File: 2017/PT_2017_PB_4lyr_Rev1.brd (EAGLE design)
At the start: 162.5 x 209.5 mm, 162 parts, among them J1 APP_2POS_CONFIG12V_VERT, J2 APP_2POS_CONFIG12V_VERT, J3 APP_2POS_CONFIG12V_VERT, J4 APP_2POS_CONFIG12V_VERT, Q1 Q_IRFS7437PbF, Q10 MOSFET-NCHANNELFDD8780, Q11 MOSFET-NCHANNELFDD8780, Q12 2N7002, Q13 2N7002PW, Q2 Q_IRFS7437PbF, Q3 Q_IRFS7437PbF, Q4 Q_IRFS7437PbF, Q5 Q_IRFS7437PbF, Q6 Q_IRFS7437PbF, Q7 Q_IRFS7437PbF, Q8 MOSFET-NCHANNELFDD8780, Q9 MOSFET-NCHANNELFDD8780, U1 LT1910, U10 ACS722LLCTR-40AU-T, U11 ACS722LLCTR-40AU-T, U12 ACS722LLCTR-40AU-T, U13 ACS722LLCTR-40AU-T, U14 ACS722LLCTR-40AU-T, U15 LM5050, U16 LM5050, U17 LM5050, U18 LM5050, U19 ACS722LLCTR-40AU-T, U2 LT1910, U20 ACS722LLCTR-40AU-T, U21 ACS722LLCTR-40AU-T, U22 ACS722LLCTR-40AU-T, U24 MAX3077, U3 LT1910, U4 LT1910, U5 LT1910, U6 LT1910, U7 LT1910, U8 ACS722LLCTR-40AU-T, U9 ACS722LLCTR-40AU-T, X1 22-23-2021

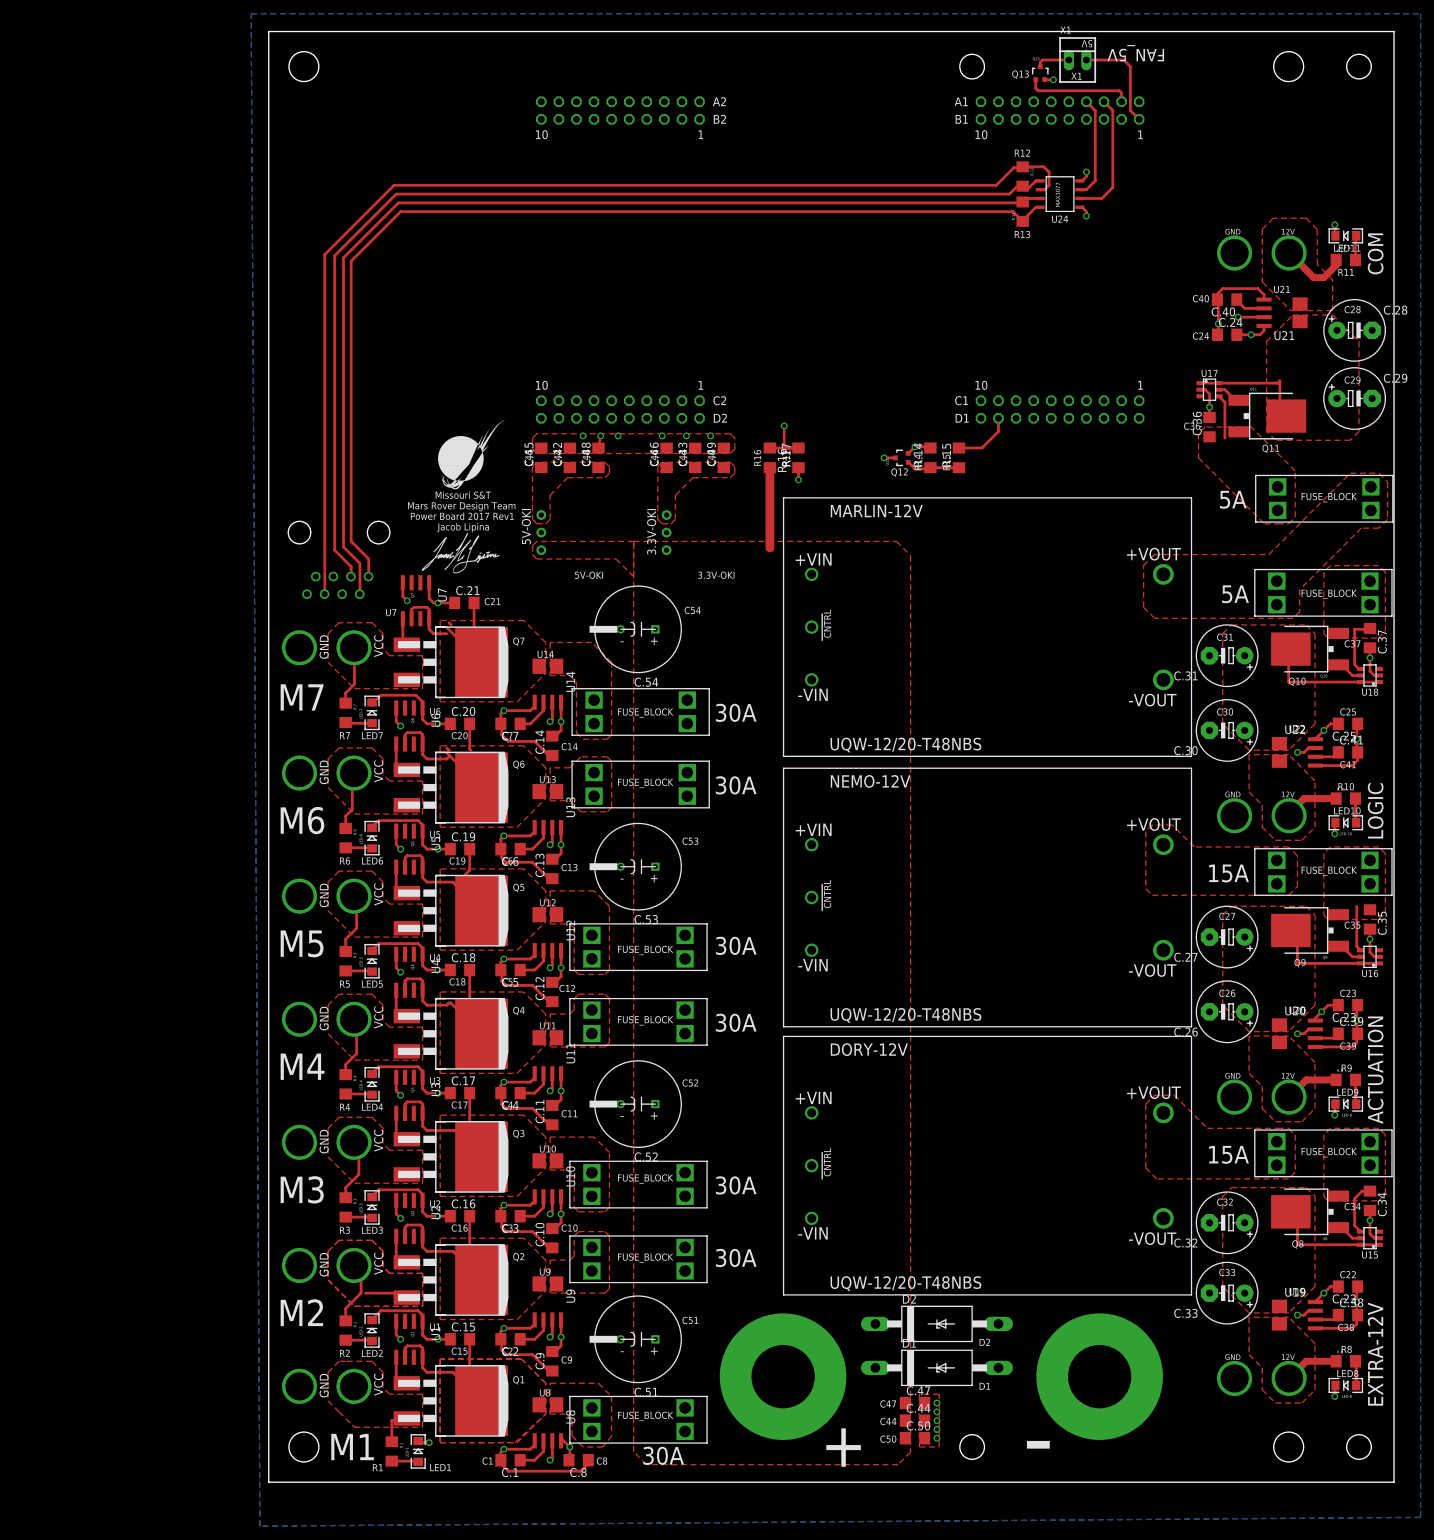
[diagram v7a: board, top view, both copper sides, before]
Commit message: Completed All Changes Adressed in Board Review
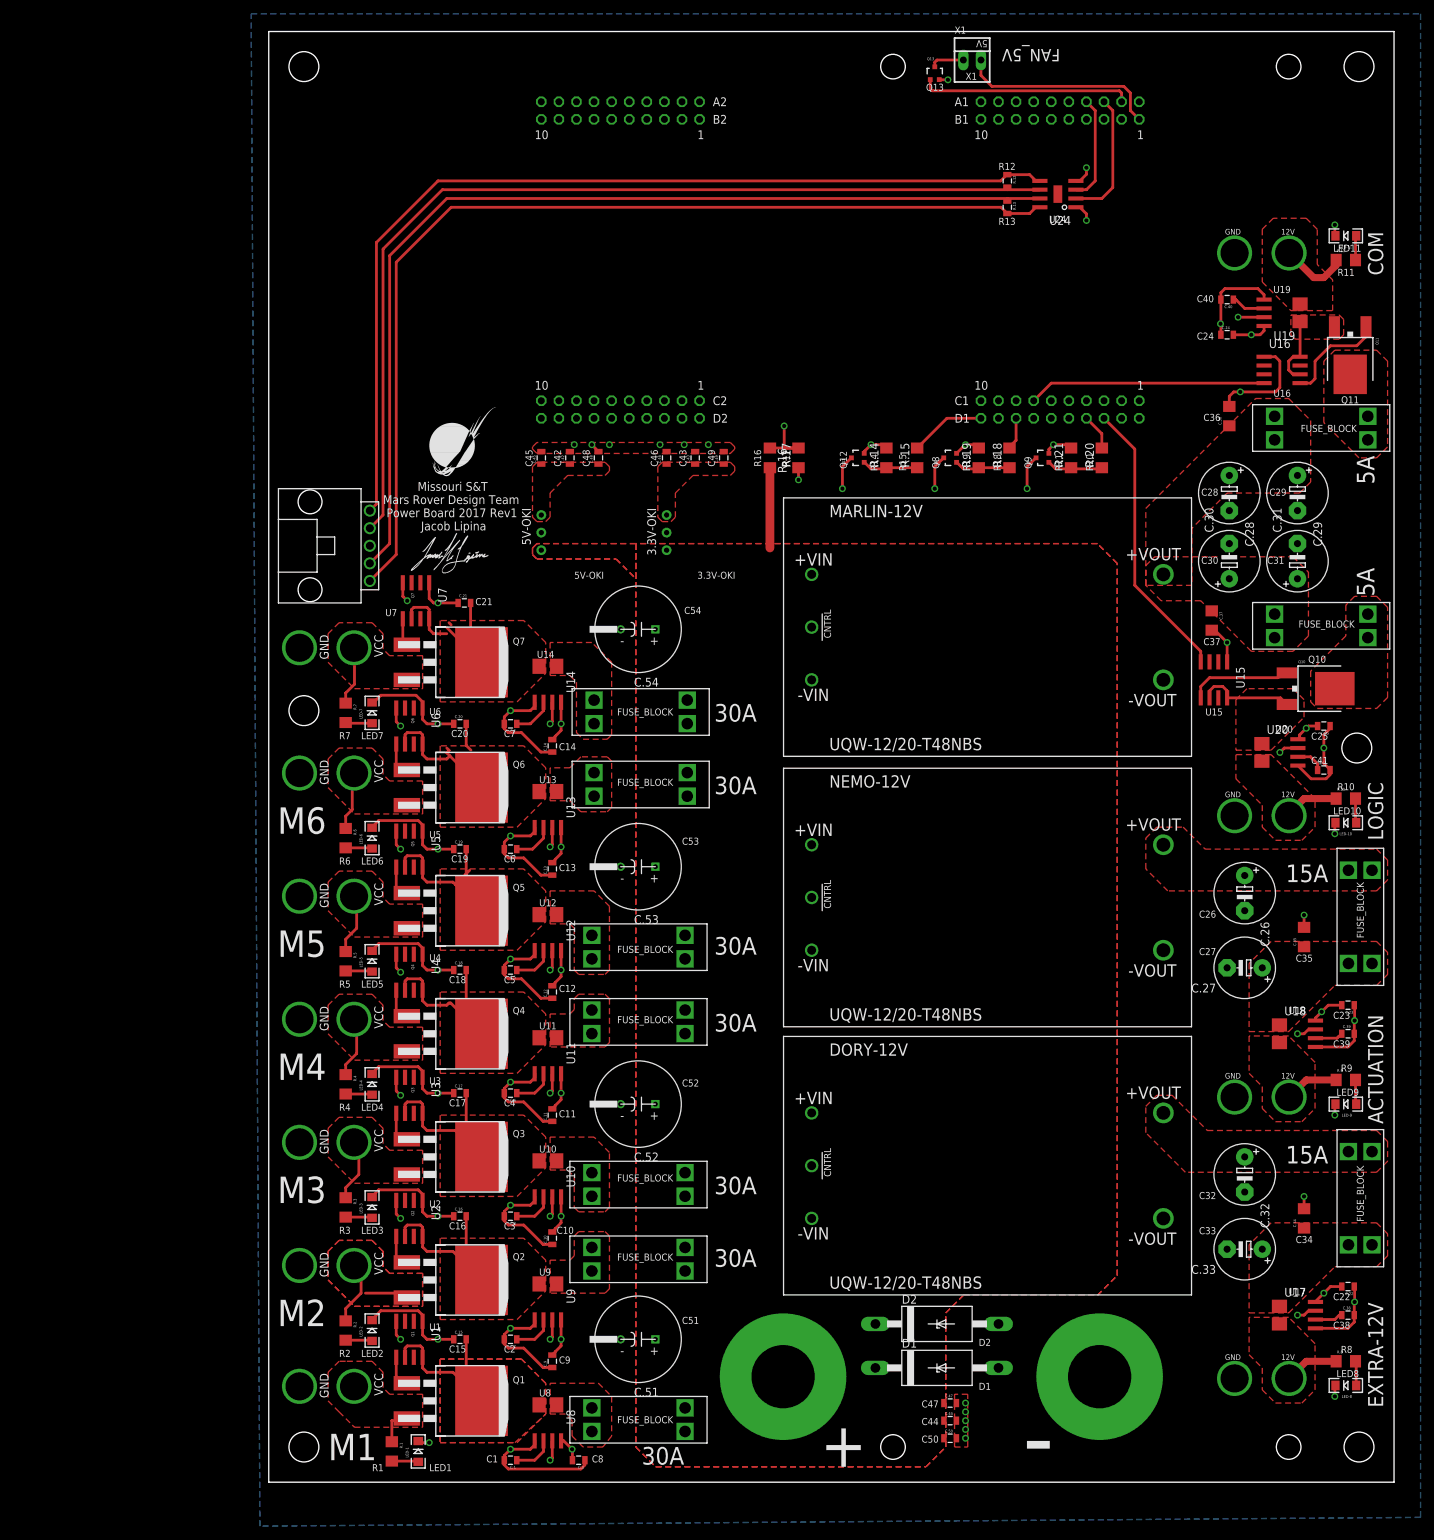
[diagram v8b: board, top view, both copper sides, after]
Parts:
- removed RJ45: RJ45KEYSTONE-949, MRDT-2015-General:KEYSTONE-949
- removed U21, U22: ACS722LLCTR-40AU-T, MRDT-2015-PowerBoard:SOIC8_ACS711
- added R.18, R.20: 1k, resistor:R1206
- added R.19, R.21: 100k, resistor:R1206
- added U$4, U$9: MOUNTING_HOLE#8, MRDT-Hardware:#8_SCREW
- added U$6: 5PIN, Molex-SL:5PIN
- C.1, C.10, C.11, C.12, C.13, C.14, C.15, C.16, C.17, C.18, C.19, C.2, C.20, C.21, C.22, C.23, C.24, C.25, C.3, C.38, C.39, C.4, C.40, C.41, C.42, C.43, C.44, C.45, C.46, C.47, C.48, C.49, C.5, C.50, C.6, C.7, C.8, C.9: device resistor:C1206 -> SparkFun-Capacitors:0805
- C.34, C.35, C.36, C.37: value 47uF -> 2.2uF; device resistor:C1206 -> SparkFun-Capacitors:1206
- Q8, Q9: value MOSFET-NCHANNELFDD8780 -> 2N7002; device SparkFun-DiscreteSemi:DPAK -> SparkFun-DiscreteSemi:SOT323
- R.12, R.13: value 120 Ohm -> 120; device SparkFun-Passives:1206 -> SparkFun-Passives:0805
- U15, U16: value LM5050 -> LT1910; device LM5050:LM5050 -> Jake:SO8
- U17, U18: value LM5050 -> ACS722LLCTR-40AU-T; device LM5050:LM5050 -> MRDT-2015-PowerBoard:SOIC8_ACS711
- U24: device MAX3077:MAX3070E -> MRDT-2015-General:SO8
- moved U19 144.8 mm to (146.4, 168.9), turned to 90 degrees
- moved U17 134.3 mm to (148.6, 24.1)
- moved Q8 120.2 mm to (98.4, 148.0)
- moved U16 85.7 mm to (146.4, 160.7), turned to 270 degrees
- moved U15 83.7 mm to (136.5, 115.9), turned to 180 degrees
- moved Q9 77.9 mm to (111.8, 148.0)
- moved U18 52.8 mm to (148.6, 64.8), turned to 270 degrees
- moved U20 40.7 mm to (146.1, 105.4)
- moved C.28 29.7 mm to (138.7, 142.9), turned to 270 degrees
- moved C.30 24.4 mm to (138.7, 133.0), turned to 90 degrees
- moved C.37 23.0 mm to (136.2, 124.5)
- moved U$31 19.7 mm to (161.9, 148.9), turned to 180 degrees
- moved C.26 17.3 mm to (141.0, 85.1), turned to 270 degrees
- moved C.31 17.0 mm to (148.6, 133.0), turned to 90 degrees
- moved C.29 16.0 mm to (148.6, 142.9), turned to 270 degrees
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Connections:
- removed net ACT-12V-SIG: U$1.PE2, U20.7
- removed net COM-12V-SIG: U$1.PE1, U22.7
- removed net EXTRA-12V-SIG: U$1.PE3, U19.7
- removed net LOGIC-12V-SIG: U$1.PE0, U21.7
- removed net N$11: C.32.+, C.33.+, Q8.4, U15.P$4, U15.P$5, U19.1
- removed net N$13: C.36.1, Q11.3, U$31.OUT_1, U$31.OUT_2, U17.P$6
- removed net N$14: C.26.+, C.27.+, Q9.4, U16.P$4, U16.P$5, U20.1
- removed net N$24: MARLIN-12V.8, U$31.IN_1, U$31.IN_2, U$32.IN_1, U$32.IN_2
- removed net REC+1: R.13.1, RJ45.P$1, U24.A
- removed net REC-1: R.13.2, RJ45.P$2, U24.B
- removed net SIG-12V: R.15.2, U$1.PN3
- removed net TRANS+1: R.12.2, RJ45.P$3, U24.Y
- removed net TRANS-1: R.12.1, RJ45.P$6, U24.Z
- new net ACT-CTL: R.18.2, U$1.PN2
- new net COM-SIG: U$1.PL0, U16.4
- new net COM/LOGIC-CTL: R.15.2, U$1.PP2
- new net EXTRA-CTL: R.20.2, U$1.PH3
- new net IMEAS-ACT: U$1.PE2, U18.7
- new net IMEAS-COM: U$1.PE0, U19.7
- new net IMEAS-EXTRA: U$1.PE3, U17.7
- new net IMEAS-LOGIC: U$1.PE1, U20.7
- new net LOGIC-SIG: U$1.PH2, U15.4
- new net N$18: C.27.+, C.35.1, U$30.OUT_1, U$30.OUT_2, U18.1
- new net N$25: Q8.1, R.18.1, R.19.1
- new net N$26: R.13.2, U$6.5, U24.8
- new net N$27: Q9.1, R.20.1, R.21.1
- new net N$28: Q10.1, U15.5
- new net N$29: R.13.1, U$6.4, U24.7
- new net N$30: R.12.2, U$6.2, U24.6
- new net N$31: R.12.1, U$6.1, U24.5
- net 12V-AUX-ACT: now also U18.4; no longer U20.4
- net 12V-AUX-COM: now also U20.4; no longer U22.4
- net 12V-AUX-EXTRA: now also U17.4; no longer U19.4
- net 12V-AUX-LOGIC: now also U19.4; no longer U21.4
- net 3.3V: now also U17.8, U18.8, U24.1; no longer U21.8, U22.8, U24.VCC
- net GND: now also Q8.2, Q9.2, R.19.2, R.21.2, U$6.3, U15.1, U16.1, U17.5, U18.5, U24.4; no longer RJ45.P$7, RJ45.P$8, U15.P$1, U16.P$1, U17.P$1, U18.P$1, U21.5, U22.5, U24.GND
- net N$1: now also C.26.+, NEMO-12V.8, U$30.IN_1, U$30.IN_2; no longer C.35.1, Q9.3, U$30.OUT_1, U$30.OUT_2, U16.P$6
- net N$10: now also U17.6; no longer U19.6
- net N$12: now also U18.6; no longer U20.6
- net N$15: now also U19.6; no longer U21.6
- net N$17: now also U16.5; no longer U17.P$2
- net N$19: now also Q11.3, U16.6, U16.8, U19.1; no longer C.28.+, C.29.+, Q11.4, U17.P$4, U17.P$5, U21.1
- net N$2: now also C.33.+, U17.1; no longer Q8.3, U15.P$6
- net N$20: now also Q11.4, U$31.OUT_1, U$31.OUT_2; no longer Q10.1, U18.P$2
- net N$21: now also Q10.4, U$32.OUT_1, U$32.OUT_2; no longer NEMO-12V.8, U$30.IN_1, U$30.IN_2
- net N$22: now also Q10.3, U15.6, U15.8, U20.1; no longer C.30.+, C.31.+, Q10.4, U18.P$4, U18.P$5, U22.1
- net N$23: now also C.32.+
- net N$3: now also MARLIN-12V.2, Q12.3; no longer Q9.1, U16.P$2
- net N$4: now also U20.6; no longer U22.6
- net N$5: now also DORY-12V.2, Q9.3; no longer Q8.1, U15.P$2
- net N$8: now also Q8.3; no longer DORY-12V.2, MARLIN-12V.2, Q12.3
- net N$9: now also C.28.+, C.29.+, C.30.+, C.31.+, C.36.1, MARLIN-12V.8, U$31.IN_1, U$31.IN_2, U$32.IN_1, U$32.IN_2; no longer Q10.3, U$32.OUT_1, U$32.OUT_2, U18.P$6
- net RX1: now also U24.2; no longer U24.RO
- net TX1: now also U24.3; no longer U24.DI
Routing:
- net EXTRA-12V-SIG: track 200.7 -> 0.00 mm, vias 1 -> 0
- net IMEAS-EXTRA: track 0.00 -> 199.7 mm, vias 0 -> 1
- net TRANS-1: track 162.7 -> 0.00 mm
- net ACT-12V-SIG: track 159.0 -> 0.00 mm, vias 1 -> 0
- net IMEAS-ACT: track 0.00 -> 158.0 mm, vias 0 -> 1
- net TRANS+1: track 154.3 -> 0.00 mm
- net REC-1: track 153.9 -> 0.00 mm
- net REC+1: track 150.6 -> 0.00 mm
- net N$26: track 0.00 -> 144.6 mm
- net N$29: track 0.00 -> 143.3 mm
- net N$30: track 0.00 -> 140.0 mm
- net N$31: track 0.00 -> 139.4 mm
- net N$5: track 3.86 -> 129.8 mm, vias 0 -> 1
- net COM-12V-SIG: track 117.3 -> 0.00 mm, vias 1 -> 0
- net IMEAS-LOGIC: track 0.00 -> 114.8 mm, vias 0 -> 1
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- added copper zone on layer 1, net N$18
- added copper zone on layer 1, net N$20
- added copper zone on layer 2, net V_BATT
- removed copper zone on layer 1, net N$11
- removed copper zone on layer 1, net N$13
- removed copper zone on layer 1, net N$14
- removed copper zone on layer 1, net N$24
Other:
- board text added: "R18"
- board text added: "R19"
- board text added: "R20"
- board text added: "R21"
- board text removed: "M7"
- board text removed: "U21"
- board text removed: "U22"
